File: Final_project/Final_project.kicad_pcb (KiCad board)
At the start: 2 copper layers, 57 parts, among them J1 USB4105-GF-A, J2 Conn_01x04, J3 DEBUG, J4 LEFT, J5 RIGHT, U1 RP2040, U2 MCP1702T-3302E_CB, U3 W25Q128JV, U4 ESP32-WROOM-32, U5 LM393D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

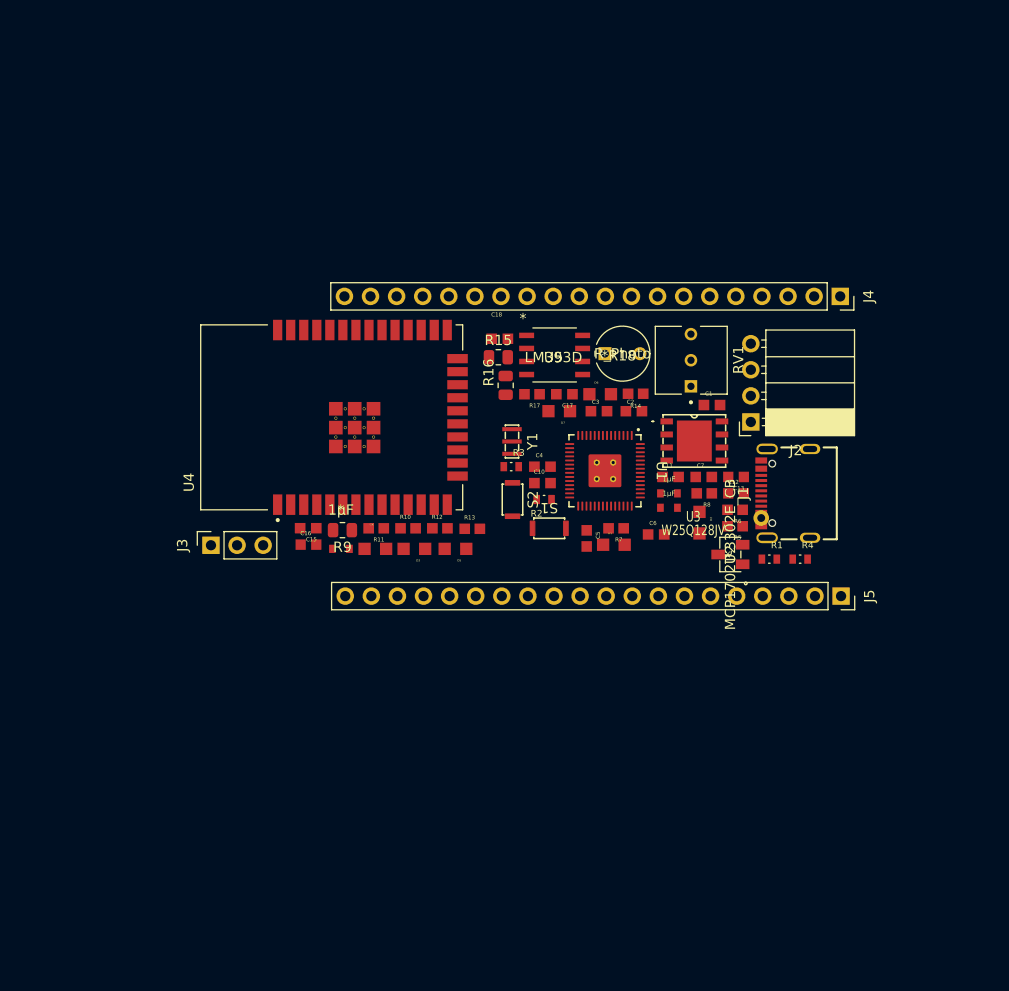
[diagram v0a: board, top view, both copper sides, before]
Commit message: Fix 3V3 label, fix USB footprint, layout begin
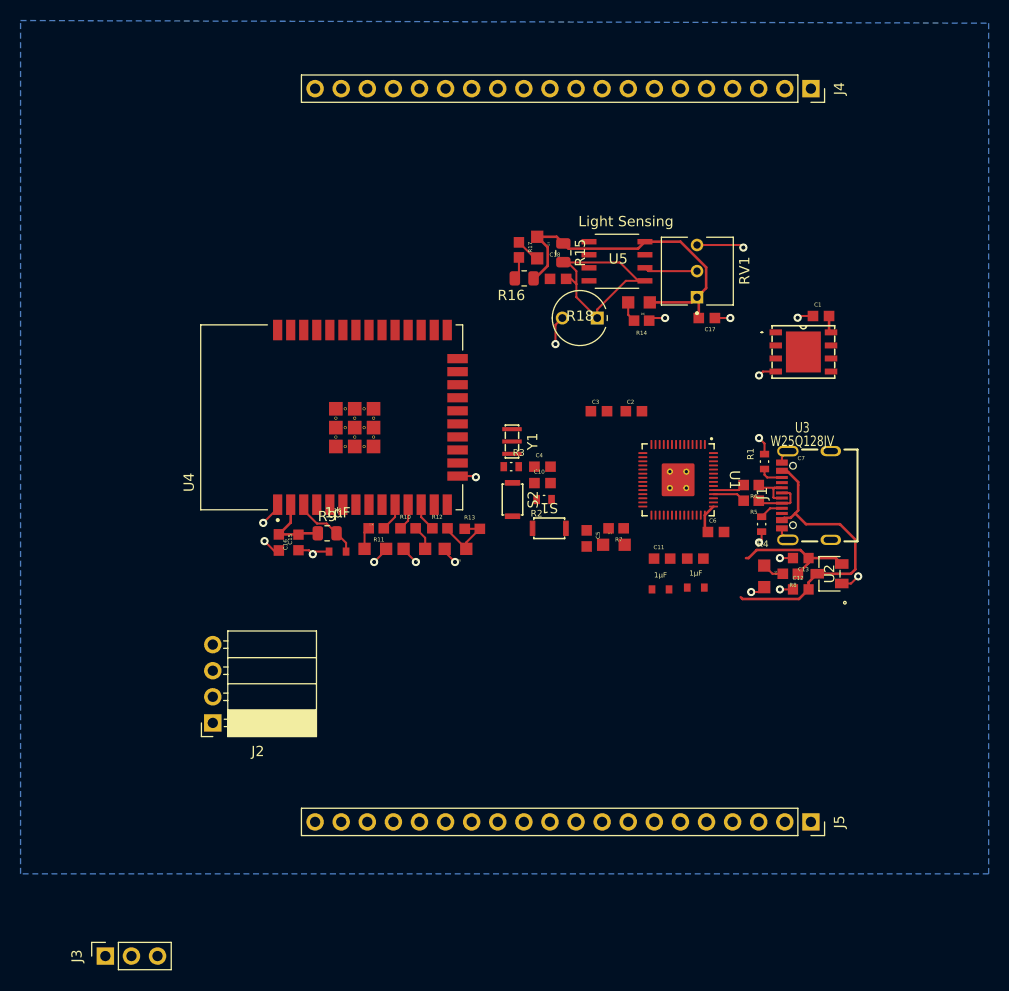
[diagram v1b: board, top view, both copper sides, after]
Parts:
- moved J2 60.0 mm to (92.6, 104.9)
- moved J3 41.3 mm to (82.2, 127.6)
- moved J5 22.2 mm to (150.8, 114.6)
- moved J4 20.4 mm to (150.8, 43.2)
- moved D7 16.1 mm to (124.2, 58.7), turned to -90 degrees
- moved C17 15.7 mm to (140.7, 65.5)
- moved R17 14.1 mm to (122.4, 58.9), turned to -90 degrees
- moved C1 13.7 mm to (151.8, 65.3)
- moved U3 13.7 mm to (150.1, 68.8)
- moved R15 12.0 mm to (126.7, 59.2), turned to -90 degrees
- moved R8 11.5 mm to (148.8, 90.4)
- moved C12 11.3 mm to (149.9, 91.9)
- moved U5 11.0 mm to (132.0, 60.0), turned to 180 degrees
- moved R16 10.6 mm to (122.9, 61.7), turned to 180 degrees
- moved C13 10.1 mm to (149.9, 88.9)
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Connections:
- R9 pad 1: +3.3V -> +3V3
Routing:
- net +3V3: track 0.00 -> 57.6 mm
- net GND: track 0.00 -> 39.9 mm, vias 0 -> 19
- net /VBUS: track 0.00 -> 29.4 mm
- net /Light_Sensing/AO: track 0.00 -> 23.6 mm
- net /GPIO15: track 0.00 -> 6.83 mm
- net Net-(D5-Pad2): track 0.00 -> 6.72 mm
- net Net-(RV1-Pad2): track 0.00 -> 5.20 mm
- net Net-(J1-PadA6): track 0.00 -> 4.93 mm
- net Net-(J1-PadA7): track 0.00 -> 4.92 mm
- net Net-(R5-Pad2): track 0.00 -> 3.20 mm
- net Net-(R6-Pad2): track 0.00 -> 3.14 mm
- net /WiFi_Module/GREEN: track 0.00 -> 2.76 mm
- net /WiFi_Module/BLUE: track 0.00 -> 2.75 mm
- net /WiFi_Module/RED: track 0.00 -> 2.61 mm
- net Net-(D7-Pad1): track 0.00 -> 2.42 mm
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- added copper zone on B.Cu, net GND
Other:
- board text added: "Light Sensing"

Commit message: Layout continued, delete header
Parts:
- removed J3: DEBUG, Connector_PinSocket_2.54mm:PinSocket_1x03_P2.54mm_Vertical
- removed J4: LEFT, Connector_PinSocket_2.54mm:PinSocket_1x20_P2.54mm_Vertical
- removed J5: RIGHT, Connector_PinSocket_2.54mm:PinSocket_1x20_P2.54mm_Vertical
- moved J2 69.4 mm to (150.8, 67.1)
- moved Y1 10.7 mm to (131.8, 81.3)
- moved C5 8.79 mm to (137.8, 86.5), turned to 0 degrees
- moved C1 8.00 mm to (144.9, 69.3)
- moved U3 7.86 mm to (143.4, 72.9)
- moved D1 6.08 mm to (131.9, 93.7)
- moved R7 6.08 mm to (132.1, 92.1)
- moved C7 5.61 mm to (144.3, 85.9), turned to -90 degrees
- moved C18 0.63 mm to (126.7, 62.1)
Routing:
- net +3V3: track 57.6 -> 87.6 mm
- net /GPIO0: track 2.20 -> 21.2 mm
- net /BOOT: track 0.00 -> 13.3 mm
- net Net-(U1-Pad51): track 0.00 -> 13.1 mm
- net GND: track 39.9 -> 53.0 mm, vias 19 -> 26
- net Net-(U1-Pad52): track 0.00 -> 11.1 mm
- net Net-(U1-Pad55): track 0.00 -> 10.9 mm
- net Net-(U1-Pad54): track 0.00 -> 9.76 mm
- net Net-(U1-Pad53): track 0.00 -> 7.69 mm
- net /RUN: track 0.00 -> 3.57 mm
- net Net-(U1-Pad21): track 0.00 -> 3.24 mm
- net Net-(C10-Pad1): track 0.00 -> 3.13 mm
- net Net-(U1-Pad20): track 0.00 -> 2.91 mm
- net Net-(D1-Pad2): track 0.00 -> 1.82 mm
- net /Light_Sensing/AO: track 23.6 -> 21.9 mm
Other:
- board text added: "3V3"
- board text added: "D0"
- board text added: "Vin"

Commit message: almost finished layout
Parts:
- moved D7 15.8 mm to (126.2, 74.3), turned to 180 degrees
- moved C17 15.6 mm to (126.9, 72.7)
- moved R17 13.9 mm to (123.7, 72.7), turned to 180 degrees
- moved C12 12.3 mm to (143.6, 81.4)
- moved R15 12.0 mm to (120.4, 69.3), turned to 0 degrees
- moved C13 11.3 mm to (144.3, 79.1), turned to -90 degrees
- moved R8 11.2 mm to (140.5, 83.0)
- moved U2 10.7 mm to (142.4, 87.2)
- moved Y1 10.7 mm to (121.8, 77.5)
- moved R16 10.6 mm to (121.1, 72.1), turned to 90 degrees
- moved U5 10.5 mm to (126.0, 68.7), turned to 0 degrees
- moved J2 10.3 mm to (145.0, 75.7)
- moved D6 9.71 mm to (130.3, 73.0), turned to 0 degrees
- moved C9 9.18 mm to (137.3, 82.9)
- moved R1 9.10 mm to (147.7, 88.5), turned to 180 degrees
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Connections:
- R9 pad 1: +3V3 -> +3.3V
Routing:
- net GND: track 53.0 -> 157.4 mm, vias 26 -> 5
- net +3V3: track 87.6 -> 143.9 mm, vias 0 -> 10
- net /GPIO11: track 0.00 -> 32.4 mm
- net /GPIO12: track 0.00 -> 30.2 mm, vias 0 -> 2
- net /GPIO15: track 6.83 -> 35.7 mm, vias 0 -> 2
- net /GPIO10: track 0.00 -> 26.9 mm
- net /GPIO14: track 0.00 -> 25.2 mm, vias 0 -> 2
- net /GPIO13: track 0.00 -> 22.4 mm, vias 0 -> 2
- net /GPIO2: track 0.00 -> 17.4 mm
- net Net-(C10-Pad1): track 3.13 -> 19.8 mm
- net /GPIO3: track 0.00 -> 13.8 mm, vias 0 -> 1
- net Net-(RV1-Pad2): track 5.20 -> 16.5 mm
- net /Light_Sensing/AO: track 21.9 -> 13.7 mm
- net /BOOT: track 13.3 -> 21.2 mm, vias 0 -> 2
- net Net-(U1-Pad55): track 10.9 -> 3.48 mm
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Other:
- board outline added: 66 x 25.1 mm
- board text removed: "3V3"
- board text removed: "D0"
- board text removed: "Light Sensing"
- board text removed: "Vin"

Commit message: updated pcb file
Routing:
- net GND: track 157.4 -> 167.6 mm
- net /GPIO3: track 13.8 -> 15.3 mm, vias 1 -> 2
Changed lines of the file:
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@@
   (segment (start 102.136 88.864) (end 100.228 88.864) (width 0.508) (layer "F.Cu") (net 1))
   (segment (start 118.973 79.773) (end 121.196 77.55) (width 0.381) (layer "F.Cu") (net 1))
+  (segment (start 104.605 76.2) (end 104.605 77.1175) (width 0.508) (layer "F.Cu") (net 1))
   (segment (start 125.95 78.55) (end 125.95 78.3) (width 0.2) (layer "F.Cu") (net 1))
   (segment (start 102.7 87.9) (end 102.7 88.3) (width 0.508) (layer "F.Cu") (net 1))
@@
   (segment (start 135.974 87.964) (end 136.568 87.37) (width 0.508) (layer "F.Cu") (net 1))
   (segment (start 121.196 77.55) (end 121.75 77.55) (width 0.381) (layer "F.Cu") (net 1))
+  (segment (start 108.275 74.365) (end 108.275 75.2825) (width 0.508) (layer "F.Cu") (net 1))
   (segment (start 142.8 81.156261) (end 142.8 81.4) (width 0.508) (layer "F.Cu") (net 1))
   (segment (start 139.316 73.5) (end 137.7 73.5) (width 0.508) (layer "F.Cu") (net 1))
@@
   (segment (start 139.4 77.1) (end 139.4 73.584) (width 0.508) (layer "F.Cu") (net 1))
   (segment (start 142.8 81.4) (end 141.2 81.4) (width 0.508) (layer "F.Cu") (net 1))
+  (segment (start 104.605 77.1175) (end 104.605 78.035) (width 0.508) (layer "F.Cu") (net 1))
   (segment (start 144.3 79.818) (end 144.3 79.9) (width 0.508) (layer "F.Cu") (net 1))
   (segment (start 130.3945 71.9595) (end 130.07865 71.9595) (width 0.381) (layer "F.Cu") (net 1))
@@
   (segment (start 146.585 78.825) (end 146.01 79.4) (width 0.508) (layer "F.Cu") (net 1))
   (segment (start 136.568 87.37) (end 136.568 87) (width 0.508) (layer "F.Cu") (net 1))
+  (segment (start 108.275 77.1175) (end 108.275 76.2) (width 0.508) (layer "F.Cu") (net 1))
   (segment (start 119.782 66.868) (end 120.45 66.2) (width 0.508) (layer "F.Cu") (net 1))
   (segment (start 128.67415 70.555) (end 127.635 71.59415) (width 0.508) (layer "F.Cu") (net 1))
+  (segment (start 104.605 74.365) (end 104.605 76.2) (width 0.508) (layer "F.Cu") (net 1))
   (segment (start 150.765 87.915) (end 151.35 88.5) (width 0.508) (layer "F.Cu") (net 1))
+  (segment (start 146.585 86.585) (end 146.216 86.216) (width 0.508) (layer "F.Cu") (net 1))
   (segment (start 118.973 79.773) (end 118.973 80.423) (width 0.381) (layer "F.Cu") (net 1))
+  (segment (start 106.44 78.035) (end 108.275 78.035) (width 0.508) (layer "F.Cu") (net 1))
   (segment (start 140.050001 88.150001) (end 143.5952 88.150001) (width 0.508) (layer "F.Cu") (net 1))
   (segment (start 138.1 82.9) (end 138.1 84.1556) (width 0.508) (layer "F.Cu") (net 1))
@@
   (segment (start 139.4 86.75) (end 139.4 87.5) (width 0.508) (layer "F.Cu") (net 1))
   (segment (start 130.3945 71.9595) (end 131.553999 70.800001) (width 0.381) (layer "F.Cu") (net 1))
+  (segment (start 146.585 86.92) (end 146.585 86.585) (width 0.508) (layer "F.Cu") (net 1))
   (segment (start 146.95 87.285) (end 146.585 86.92) (width 0.508) (layer "F.Cu") (net 1))
   (segment (start 98.94 83.7) (end 98.94 82.612) (width 0.508) (layer "F.Cu") (net 1))
@@
   (segment (start 98.94 82.612) (end 103.517 78.035) (width 0.508) (layer "F.Cu") (net 1))
   (segment (start 129.02 87.768) (end 129.02 88.108) (width 0.508) (layer "F.Cu") (net 1))
+  (segment (start 106.44 76.2) (end 105.5225 76.2) (width 0.508) (layer "F.Cu") (net 1))
   (segment (start 131 74.6) (end 130.3945 73.9945) (width 0.381) (layer "F.Cu") (net 1))
   (segment (start 118.973 80.423) (end 119.25 80.7) (width 0.381) (layer "F.Cu") (net 1))
@@
   (segment (start 127.635 71.59415) (end 127.635 72.7) (width 0.508) (layer "F.Cu") (net 1))
   (segment (start 146.01 79.4) (end 144.718 79.4) (width 0.508) (layer "F.Cu") (net 1))
+  (segment (start 146.216 86.216) (end 146.01 86.216) (width 0.508) (layer "F.Cu") (net 1))
   (segment (start 98.94 84.788) (end 98.94 83.7) (width 0.508) (layer "F.Cu") (net 1))
   (segment (start 131.553999 70.800001) (end 132.6 70.800001) (width 0.381) (layer "F.Cu") (net 1))
@@
   (segment (start 105.4262 89.054) (end 108.446 89.054) (width 0.508) (layer "F.Cu") (net 1))
   (segment (start 126.8 79.4) (end 125.95 78.55) (width 0.2) (layer "F.Cu") (net 1))
+  (segment (start 105.5225 74.365) (end 104.605 74.365) (width 0.508) (layer "F.Cu") (net 1))
   (via (at 137.7 73.5) (size 0.3048) (drill 0.4) (layers "F.Cu" "B.Cu") (net 1))
   (via (at 120.45 66.2) (size 0.3048) (drill 0.4) (layers "F.Cu" "B.Cu") (net 1))
@@
   (segment (start 146.75 84.027818) (end 148.4 85.677818) (width 0.2) (layer "B.Cu") (net 18))
   (segment (start 143.65 74.3) (end 145 75.65) (width 0.2) (layer "F.Cu") (net 20))
-  (segment (start 131.8 76.27141) (end 131.8 76.9625) (width 0.2) (layer "F.Cu") (net 20))
+  (segment (start 132.25 75.7) (end 131.8 76.15) (width 0.2) (layer "F.Cu") (net 20))
+  (segment (start 131.8 76.15) (end 131.8 76.9625) (width 0.2) (layer "F.Cu") (net 20))
   (segment (start 142.7 74.3) (end 143.65 74.3) (width 0.2) (layer "F.Cu") (net 20))
+  (via (at 132.25 75.7) (size 0.3048) (drill 0.4) (layers "F.Cu" "B.Cu") (net 20))
   (via (at 142.7 74.3) (size 0.3048) (drill 0.4) (layers "F.Cu" "B.Cu") (net 20))
-  (segment (start 132.87141 75.2) (end 141.8 75.2) (width 0.2) (layer "B.Cu") (net 20))
-  (segment (start 141.8 75.2) (end 142.7 74.3) (width 0.2) (layer "B.Cu") (net 20))
+  (segment (start 137.183474 75.7) (end 132.25 75.7) (width 0.2) (layer "B.Cu") (net 20))
+  (segment (start 142.25 74.75) (end 138.133474 74.75) (width 0.2) (layer "B.Cu") (net 20))
+  (segment (start 138.133474 74.75) (end 137.183474 75.7) (width 0.2) (layer "B.Cu") (net 20))
+  (segment (start 142.25 74.75) (end 142.7 74.3) (width 0.2) (layer "B.Cu") (net 20))
   (segment (start 132.412096 76.225) (end 134.189 76.225) (width 0.2) (layer "F.Cu") (net 21))
   (segment (start 135.22 73.98) (end 138.469 70.731) (width 0.2) (layer "F.Cu") (net 21))

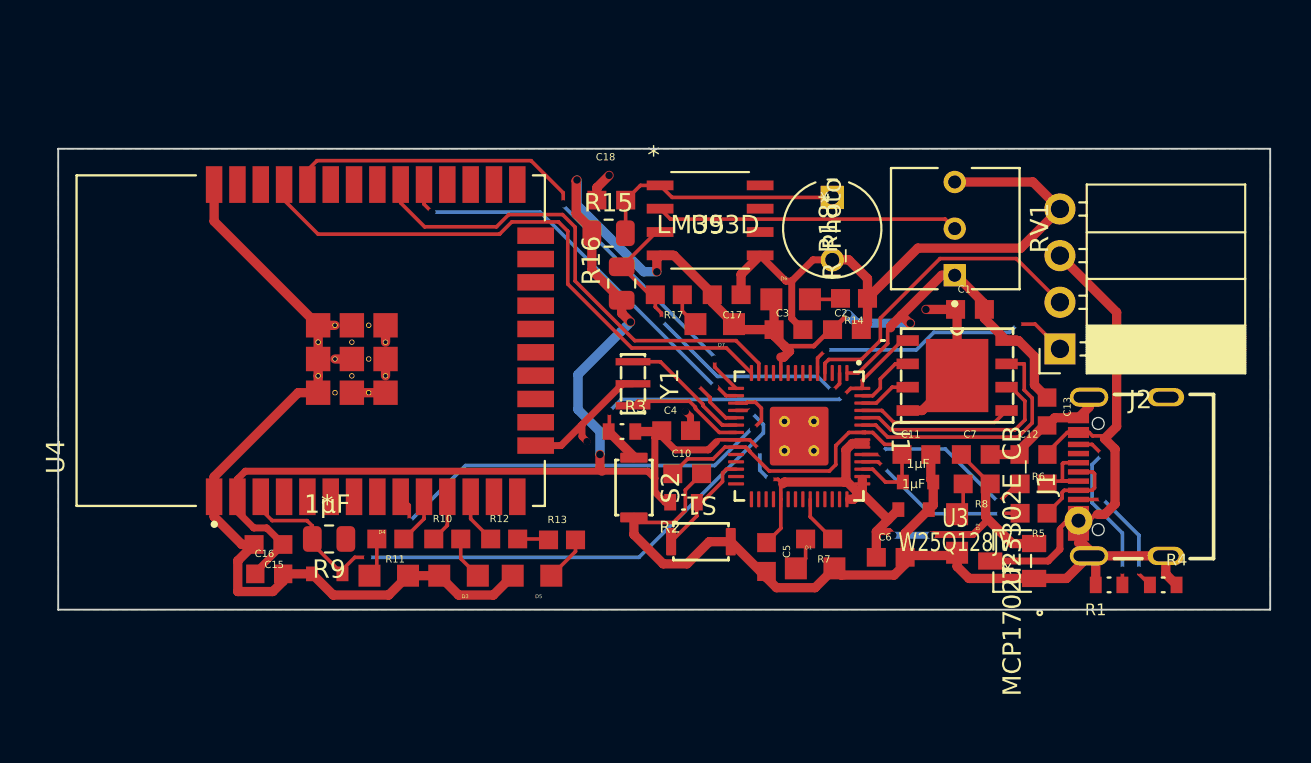
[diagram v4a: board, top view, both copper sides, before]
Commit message: finishing up layout, a few steps remained
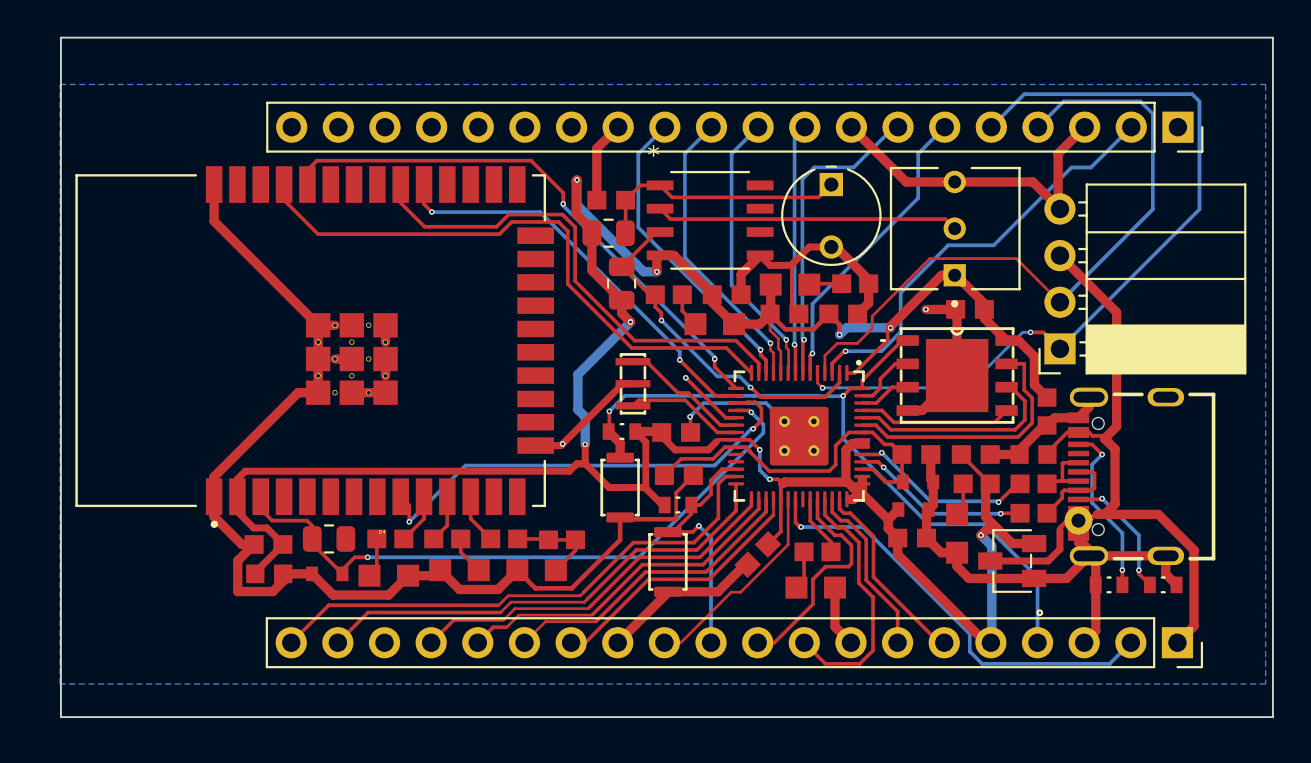
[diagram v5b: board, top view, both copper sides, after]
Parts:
- added J4: LEFT, Connector_PinSocket_2.54mm:PinSocket_1x20_P2.54mm_Vertical, F.Cu at (151.4, 63.6)
- added J5: RIGHT, Connector_PinSocket_2.54mm:PinSocket_1x20_P2.54mm_Vertical, F.Cu at (151.4, 91.7)
- moved S1 2.11 mm to (123.7, 87.2), turned to 90 degrees
- moved C6 1.57 mm to (136.9, 86.0)
- moved D1 1.05 mm to (131.7, 88.7)
- moved C3 0.88 mm to (130.0, 73.8)
- moved C2 0.87 mm to (133.2, 73.8)
- moved R14 0.80 mm to (133.8, 72.1)
- moved D6 0.80 mm to (130.3, 72.2)
- moved S2 0.75 mm to (121.0, 83.2)
- moved R7 0.71 mm to (131.8, 86.7)
- moved R18 0.70 mm to (132.6, 66.7)
- moved C5 0.49 mm to (128.6, 86.8), turned to -135 degrees
- moved C10 0.46 mm to (124.2, 82.5)
- moved D5 0.39 mm to (116.5, 87.7)
- moved R2 0.34 mm to (124.2, 84.2)
- moved D3 0.30 mm to (112.3, 87.7)
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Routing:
- net /GPIO16: track 0.00 -> 29.1 mm
- net /GPIO3: track 15.3 -> 44.3 mm
- net /GPIO17: track 0.00 -> 26.1 mm
- net /GPIO23: track 0.00 -> 23.7 mm, vias 0 -> 1
- net /GPIO1: track 0.00 -> 23.5 mm, vias 0 -> 1
- net /GPIO18: track 0.00 -> 20.9 mm
- net /GPIO2: track 17.4 -> 36.8 mm
- net /BOOT: track 21.2 -> 40.5 mm
- net /GPIO19: track 0.00 -> 18.8 mm
- net /GPIO5: track 0.00 -> 17.0 mm, vias 0 -> 1
- net /GPIO9: track 0.00 -> 16.9 mm, vias 0 -> 1
- net /GPIO20: track 0.00 -> 16.8 mm
- net /GPIO4: track 0.00 -> 16.4 mm, vias 0 -> 1
- net /GPIO8: track 0.00 -> 16.0 mm, vias 0 -> 1
- net /GPIO7: track 0.00 -> 15.3 mm, vias 0 -> 1
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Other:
- board size 66 x 25.1 mm -> 66 x 37 mm
